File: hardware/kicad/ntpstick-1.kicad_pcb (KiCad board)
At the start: 2 copper layers, 140 x 25 mm, 78 parts, among them CON1 PDI, IC1 W5500, IC2 ATXMEGA128A4-A, IC3 24AA02E48, J1 MOUNT0, J2 MOUNT1, P1 EIA 568B, P2 CONN_01X05, U1 TG110-E*N5_N5, U2 LM2672, U3 UBLOX-GPS, U4 MAX5805BAUB+, X1 25MHz, X2 VCXO-7x5

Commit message: Version 1.2 HW design
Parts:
- removed CON1: PDI, pin_array_3x2
- removed SYM: Symbol_OSHW-Logo_SilkScreen_07Jul2012, Symbols:Symbol_OSHW-Logo_SilkScreen
- removed U4: MAX5805BAUB+, SMD_Packages:MSOP10-0.5
- added C35: 100nF, SMD_Packages:SM0603, F.Cu at (150.2, 54.7)
- added D2: PWR, LEDs:LED-0805, F.Cu at (142.7, 50.0)
- added FIDUCIAL: val**, Freetronics Footprints:FIDUCIAL, F.Cu at (49.0, 51.0)
- added IC4: LMR16006, SMD_Packages:SOT23_6, F.Cu at (61.2, 63.8)
- added J3: MOUNT2, 4-40-HOLE, F.Cu at (119.4, 52.8)
- added L2: 27nH, Walter Inductors:inductor_smd_0603, F.Cu at (153.0, 57.3)
- added L4: 250mA, Walter Inductors:inductor_smd_0603, F.Cu at (143.8, 62.5)
- added LOGO_CC: VAL**, Freetronics Footprints:LOGO_CC_1.9mm, F.Cu at (83.3, 51.8)
- added LOGO_CC_BY: VAL**, CC logos:LOGO_CC_BY_1.9mm, F.Cu at (85.4, 51.8)
- added LOGO_CC_SA: VAL**, LOGO_CC_SA_1.9mm, F.Cu at (87.6, 51.8)
- added LOGO_OSHW_silkscreen_2mm: val**, Freetronics Footprints:LOGO_OSHW_silkscreen_2mm, F.Cu at (81.0, 51.8)
- added P3: PDI-SER, Pin_Headers:Pin_Header_Straight_2x05, F.Cu at (119.4, 74.4)
- added P7: 5V, Pin_Headers:Pin_Header_Straight_1x02, F.Cu at (66.0, 50.8)
- added P8: VIN, Pin_Headers:Pin_Header_Straight_1x02, F.Cu at (66.0, 73.7)
- added R16: 1k, SMD_Packages:SM0603, F.Cu at (149.7, 72.9)
- added R2: 1k, SMD_Packages:SM0603, F.Cu at (146.4, 72.9)
- added R23: 10, SMD_Packages:SM0603, F.Cu at (150.2, 57.3)
- added R26: 100k, SMD_Packages:SM0603, F.Cu at (62.7, 67.1)
- added R27: 1k, SMD_Packages:SM0603, F.Cu at (138.7, 50.0)
- added R5: 1k, SMD_Packages:SM0603, F.Cu at (148.1, 72.9)
- added SERIAL_LABEL: VAL**, Dymo 12x24:SERIAL_LABEL, B.Cu at (85.9, 62.7)
- added U5: UBLOX-MAX, UBLOX MAX:UBLOX-MAX-8-POLY, F.Cu at (150.4, 64.9)
- ANT1: value ANTENNA -> ANTENNA_SHIELD; footprint 1575AT43A0-JOHANSON -> Walter RF Conn:coaxial_u.fl-r-smt-1
- C24, C27: value 22uF -> 10uF; footprint Capacitors_SMD:c_elec_6.3x5.8 -> Water SMD Cap:c_tant_A
- C25: footprint SM0603 -> SMD_Packages:SM0603
- C28: value 22uF -> 3.3uF; footprint Capacitors_SMD:c_elec_6.3x5.8 -> SMD_Packages:SM1210
- C29: value 22uF -> 100nF; footprint Capacitors_SMD:c_elec_6.3x5.8 -> SMD_Packages:SM0603
- C30: value 10nF -> 100nF; footprint Capacitors_SMD:c_0603 -> SMD_Packages:SM0603
- C31, C32: value 22uF -> 10uF; footprint Capacitors_SMD:c_elec_4x5.3 -> Water SMD Cap:c_1206
- C33: footprint c_tant_A -> Water SMD Cap:c_tant_A
- D3: footprint DO-214AA(SMB) -> Walter Diodes:do214ac
- D4: footprint SMD_Packages:DO-214AA(SMB) -> Walter Diodes:do214ac
- D5: value PWR -> SYS
- L3: value 47uH -> 6.8uH; footprint Walter Inductors:inductor_smd_8x5mm -> Bourns Inductor:inductor_bourns_srn5040
- P2: value CONN_01X05 -> GPS; footprint Walter Pin Headers:pin_strip_5 -> Pin_Headers:Pin_Header_Straight_1x05
- R24: value NP -> 6.49k
- R25: value 0 -> 36.0k
- U2: value LM2672 -> NCP1117ST33T3G; footprint Walter SMD DIL:so-8 -> SMD_Packages:SOT223
- U3: value UBLOX-GPS -> MCP4725AxT-E/CH; footprint UBLOX-GPS -> SMD_Packages:SOT23_6
- moved C29 76.3 mm to (139.4, 61.2)
- moved U2 61.1 mm to (107.7, 52.7), turned to 270 degrees
- moved C24 47.9 mm to (101.3, 52.1)
- moved C27 47.0 mm to (114.0, 51.8), turned to 90 degrees
- moved D5 28.2 mm to (142.7, 53.0), turned to 180 degrees
- moved C32 25.4 mm to (67.6, 56.9), turned to 90 degrees
- moved C31 22.7 mm to (65.0, 56.9), turned to 90 degrees
- moved R18 18.4 mm to (129.3, 52.6)
- moved D4 18.0 mm to (66.5, 61.5)
- moved P2 17.3 mm to (137.9, 73.9)
- moved IC3 16.8 mm to (136.4, 57.9)
- moved U3 15.7 mm to (136.4, 61.5), turned to 90 degrees
- moved R22 15.6 mm to (132.1, 57.1), turned to 270 degrees
- moved ANT1 13.3 mm to (153.7, 53.7)
- moved C30 13.2 mm to (57.4, 63.0), turned to 0 degrees
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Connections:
- net /NTP Stick Ethernet/RXN renamed /NTP Stick Ethernet/RX_N
- net /NTP Stick Ethernet/RXP renamed /NTP Stick Ethernet/RX_P
- net /NTP Stick Ethernet/TXN renamed /NTP Stick Ethernet/TX_N
- net /NTP Stick Ethernet/TXP renamed /NTP Stick Ethernet/TX_P
- net Net-(C19-Pad2) renamed /NTP Stick Ethernet/RX1_P
- net Net-(C20-Pad2) renamed /NTP Stick Ethernet/RX1_N
- ANT1 pad 2: (no net) -> GND
- C24 pad 1: Net-(C24-Pad1) -> +5V
- C25 pad 1: +3.3V -> /NTP Stick System/GPS_VCC
- C27 pad 1: Net-(C24-Pad1) -> +3.3V
- C28 pad 1: Net-(C24-Pad1) -> Net-(C28-Pad1)
- C29 pad 1: Net-(C24-Pad1) -> GND
- C29 pad 2: GND -> +3.3V
- C31 pad 1: +3.3V -> +5V
- C32 pad 1: +3.3V -> +5V
- C33 pad 1: +3.3V -> /NTP Stick System/GPS_VCC
- D1 pad 1: Net-(D1-Pad1) -> +3.3V
- D1 pad 2: /NTP Stick Ethernet/LNKLED -> Net-(D1-Pad2)
- D3 pad 2: Net-(C24-Pad1) -> Net-(C28-Pad1)
- D4 pad 2: Net-(C30-Pad2) -> Net-(C30-Pad1)
- IC2 pad 21: /NTP Stick System/FACRSTn -> Net-(IC2-Pad21)
- IC2 pad 29: /NTP Stick System/GPS_TIMEPULSE -> /NTP Stick System/GPS_TP
- IC2 pad 3: Net-(IC2-Pad3) -> /NTP Stick System/LED_PWR
- IC2 pad 32: /NTP Stick System/GPS_TX -> /NTP Stick System/GPS_TXD
- IC2 pad 33: /NTP Stick System/GPS_RX -> /NTP Stick System/GPS_RXD
- L3 pad 1: Net-(C30-Pad2) -> Net-(C30-Pad1)
- L3 pad 2: +3.3V -> +5V
- P2 pad 1: +3.3V -> /NTP Stick System/GPS_RXD
- P2 pad 2: /NTP Stick System/CON_TX -> /NTP Stick System/GPS_TXD
- P2 pad 3: /NTP Stick System/CON_RX -> /NTP Stick System/GPS_TP
- P2 pad 4: /NTP Stick System/FACRSTn -> /NTP Stick System/GPS_VCC
- R18 pad 1: GND -> /NTP Stick System/LED_PWR
- R24 pad 2: Net-(R24-Pad2) -> Net-(IC4-Pad3)
- R25 pad 1: Net-(R24-Pad2) -> Net-(IC4-Pad3)
- R25 pad 2: +3.3V -> +5V
- R4 pad 1: Net-(D1-Pad1) -> /NTP Stick Ethernet/LNKLED
- R4 pad 2: +3.3V -> Net-(D1-Pad2)
- U2 pad 1: Net-(C30-Pad1) -> GND
- U2 pad 2: Net-(U2-Pad2) -> +3.3V
- U2 pad 3: Net-(U2-Pad3) -> +5V
- U3 pad 1: Net-(U3-Pad1) -> /NTP Stick System/OSC_CTRL
- U3 pad 2: Net-(U3-Pad2) -> GND
- U3 pad 3: /NTP Stick System/GPS_TIMEPULSE -> +3.3V
- U3 pad 4: Net-(U3-Pad4) -> /NTP Stick System/SDA
- U3 pad 5: Net-(U3-Pad5) -> /NTP Stick System/SCL
- U3 pad 6: Net-(U3-Pad6) -> +3.3V
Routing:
- net +3.3V: track 272.7 -> 180.7 mm, vias 2 -> 1
- net +5V: track 0.00 -> 86.0 mm
- net Net-(C24-Pad1): track 49.6 -> 0.00 mm
- net /NTP Stick System/GPS_VCC: track 0.00 -> 42.2 mm
- net /NTP Stick System/GPS_TIMEPULSE: track 37.0 -> 0.00 mm
- net /NTP Stick System/GPS_TP: track 0.00 -> 30.4 mm
- net /NTP Stick System/GPS_TX: track 29.0 -> 2.75 mm
- net /NTP Stick System/GPS_RX: track 25.6 -> 2.52 mm
- net /NTP Stick System/GPS_RXD: track 0.00 -> 22.2 mm
- net /NTP Stick System/GPS_TXD: track 0.00 -> 21.3 mm
- net Net-(C30-Pad2): track 14.4 -> 1.91 mm
- net Net-(D7-Pad2): track 2.66 -> 13.9 mm
- net Net-(C30-Pad1): track 3.07 -> 13.2 mm
- net Net-(D5-Pad2): track 2.91 -> 12.7 mm
- net Net-(C28-Pad1): track 0.00 -> 9.33 mm
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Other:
- board size 140 x 25 mm -> 113 x 30 mm
- board text added: "+V"
- board text added: "0V"
- board text added: "20150329"
- board text added: "3.0-NZ"
- board text added: "ANT SUPPLY 3V DC 50mA"
- board text added: "BY"
- board text added: "CON"
- board text added: "GND MNT"
- board text added: "GPS"
- board text added: "NTPstick 1.2"
- board text added: "PDI"
- board text added: "RX"
- board text added: "SA"
- board text added: "TIA/EIA-568B +V BLU/BLUW GND BRN/BRNW"
- board text added: "TP"
- board text added: "TX"
- board text added: "hairy.geek.nz/ntp"
- board text removed: "(C) 2014 David Zanetti CC-3.0-NZ BY-SA hairy.geek.nz/ntp"
- board text removed: "20141107"
- board text removed: "NTPstick 1.1"
- board text removed: "RESET"
- board text removed: "TIA/EIA-568B DC 7-36V +V BLU/BLUW GND BRN/BRNW"
- board text removed: "UP"

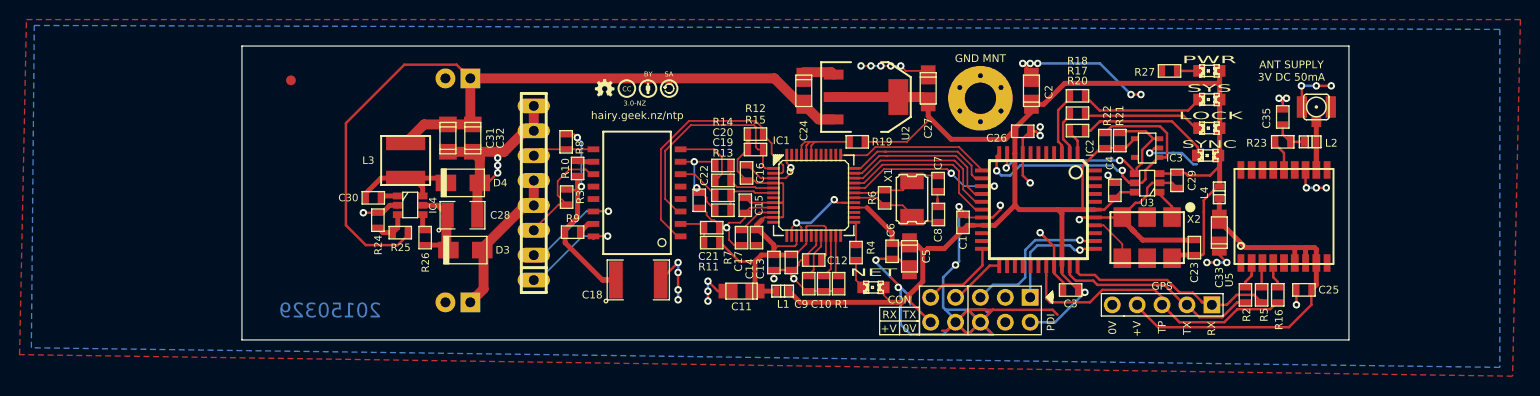
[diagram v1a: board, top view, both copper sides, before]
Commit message: Final manufactured version of 1.2 HW
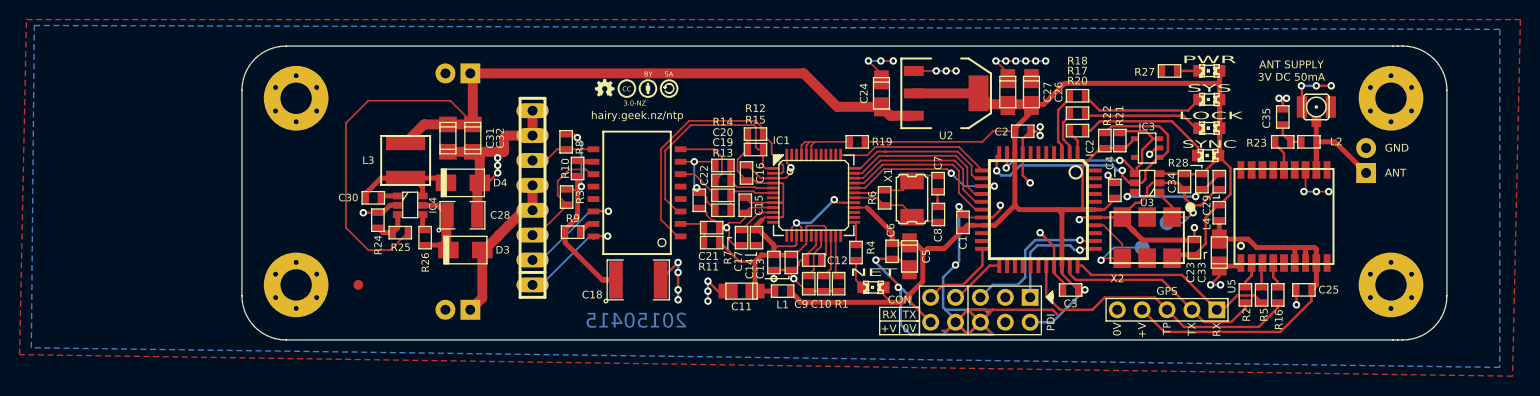
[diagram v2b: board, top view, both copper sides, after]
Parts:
- added C34: 100nF, SMD_Packages:SM0603, F.Cu at (140.2, 61.3)
- added J4: MOUNT2, Screws:4-40-HOLE, F.Cu at (161.3, 71.9)
- added P4: DAC_TEST, Measurement_Points:Measurement_Point_Round-SMD-Pad_Small, B.Cu at (138.4, 65.5)
- added P5: OSC_TEST, Measurement_Points:Measurement_Point_Round-SMD-Pad_Small, B.Cu at (135.9, 68.1)
- added P6: ANT_TEST, Pin_Headers:Pin_Header_Straight_1x02, F.Cu at (158.8, 59.2)
- added R28: NP, SMD_Packages:SM0603, F.Cu at (142.0, 61.3)
- C26: footprint c_tant_A -> Water SMD Cap:c_tant_A
- J1, J2: footprint pin_strip_1 -> Screws:4-40-HOLE
- L1: footprint inductor_smd_0603 -> SMD_Packages:SM0603
- L2, L4: footprint Walter Inductors:inductor_smd_0603 -> SMD_Packages:SM0603
- moved J3 41.9 mm to (161.3, 52.8)
- moved FIDUCIAL 22.0 mm to (55.9, 71.9)
- moved U2 8.19 mm to (115.9, 52.3)
- moved C27 8.14 mm to (122.2, 52.2)
- moved C24 7.93 mm to (109.3, 52.3)
- moved J1 4.91 mm to (49.5, 52.8)
- moved J2 4.64 mm to (49.5, 71.9)
- moved C29 4.32 mm to (143.8, 61.3)
- moved SERIAL_LABEL 2.34 mm to (84.3, 61.0)
- moved L4 2.03 mm to (143.8, 64.5)
- moved C33 2.03 mm to (143.8, 68.6)
- moved P8 0.76 mm to (66.0, 74.4)
- moved P2 0.72 mm to (138.4, 74.4)
- moved P1 0.51 mm to (73.7, 63.0)
- moved P7 0.51 mm to (66.0, 50.3)
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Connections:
- C29 pad 2: +3.3V -> Net-(C29-Pad2)
- J2 pad 1: Net-(J2-Pad1) -> GND
- L1 pad 1: /NTP Stick Ethernet/NICAVDD -> +3.3V
- L1 pad 2: +3.3V -> /NTP Stick Ethernet/NICAVDD
- U3 pad 6: +3.3V -> Net-(C29-Pad2)
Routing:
- net Net-(C29-Pad2): track 0.00 -> 11.6 mm, vias 0 -> 2
- net +5V: track 86.0 -> 94.3 mm
- net Net-(IC2-Pad37): track 5.08 -> 12.1 mm, vias 0 -> 1
- net Net-(ANT1-Pad1): track 7.77 -> 14.2 mm
- net /NTP Stick System/OSC_CTRL: track 3.25 -> 8.68 mm, vias 0 -> 1
- net +3.3V: track 180.7 -> 176.8 mm
- net GND: track 260.2 -> 257.8 mm, vias 51 -> 53
- net /NTP Stick System/GPS_TXD: track 21.3 -> 23.2 mm
- net /NTP Stick System/GPS_VCC: track 42.2 -> 40.6 mm
- net /NTP Stick System/GPS_TP: track 30.4 -> 31.8 mm
- net /NTP Stick Ethernet/TX-: track 11.9 -> 13.1 mm
- net /NTP Stick System/GPS_RXD: track 22.2 -> 22.9 mm
- net /NTP Stick Ethernet/CON_PWR: track 16.1 -> 16.8 mm
- net /NTP Stick Ethernet/TX+: track 13.0 -> 12.4 mm
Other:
- board size 113 x 30 mm -> 123 x 30 mm
- net class RF INPUT added: clearance 0.508, trace_width 0.254, via_dia 0.762, via_drill 0.381
- board text added: "20150415"
- board text added: "ANT"
- board text added: "DAC"
- board text added: "GND"
- board text added: "OSC"
- board text added: "Origins PCB edge: 1.909398425",1.87015748" Holes: 1.95",2.83""
- board text removed: "20150329"
- board text removed: "GND MNT"
